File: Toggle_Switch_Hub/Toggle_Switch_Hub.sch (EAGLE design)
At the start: 6 parts

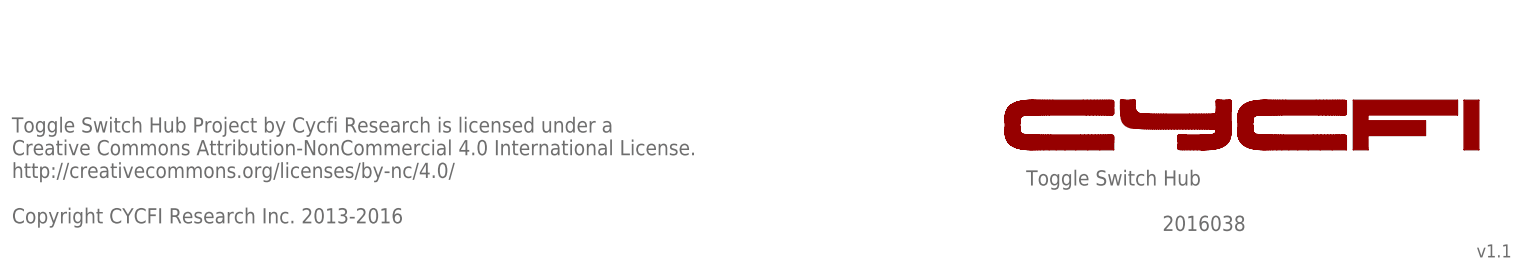
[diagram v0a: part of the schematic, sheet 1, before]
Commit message: Updated schematic licenses
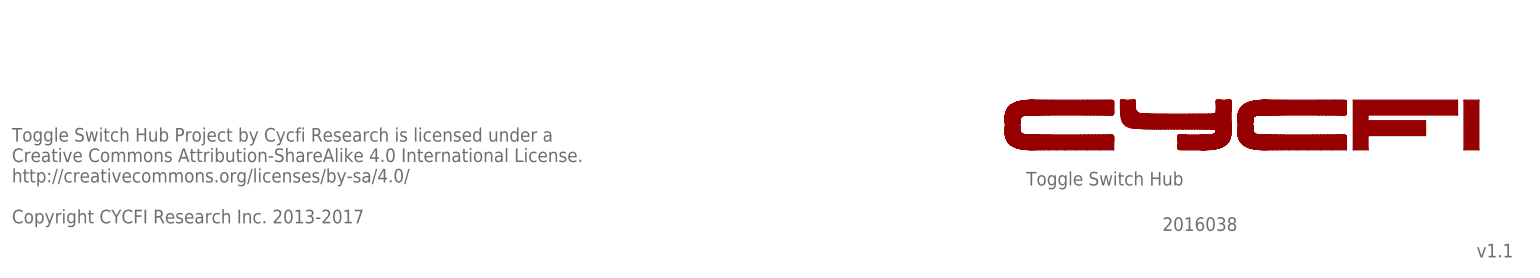
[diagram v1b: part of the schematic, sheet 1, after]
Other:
- note added: "Toggle Switch Hub Project by Cycfi Research is licensed under a Creative Commons Attribution-ShareAlike 4.0 International License. http://creativecommons.org/licenses/by-sa/4.0/ Copyright CYCFI Research Inc. 2013-2017"
- note removed: "Toggle Switch Hub Project by Cycfi Research is licensed under a Creative Commons Attribution-NonCommercial 4.0 International License. http://creativecommons.org/licenses/by-nc/4.0/ Copyright CYCFI Research Inc. 2013-2016"
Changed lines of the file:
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@@
 <text x="46.99" y="80.01" size="1.778" layer="95">STRING
 GND</text>
-<text x="177.8" y="19.05" size="2.54" layer="95">Toggle Switch Hub</text>
-<text x="253.365" y="6.985" size="2.1844" layer="95">v1.1</text>
-<text x="7.62" y="12.7" size="2.54" layer="95">Toggle Switch Hub Project by Cycfi Research is licensed under a
-Creative Commons Attribution-NonCommercial 4.0 International License.
-http://creativecommons.org/licenses/by-nc/4.0/
-Copyright CYCFI Research Inc. 2013-2016</text>
-<text x="200.66" y="11.43" size="2.54" layer="95">2016038</text>
+<text x="177.8" y="19.05" size="2.286" layer="95">Toggle Switch Hub</text>
+<text x="253.365" y="6.985" size="2.286" layer="95">v1.1</text>
+<text x="7.62" y="12.7" size="2.286" layer="95" font="fixed">Toggle Switch Hub Project by Cycfi Research is licensed under a
+Creative Commons Attribution-ShareAlike 4.0 International License.
+http://creativecommons.org/licenses/by-sa/4.0/
+Copyright CYCFI Research Inc. 2013-2017</text>
+<text x="200.66" y="11.43" size="2.286" layer="95">2016038</text>
 <wire x1="192.47528125" y1="25.047221875" x2="190.115640625" y2="25.047221875" width="0" layer="94"/>
 <wire x1="190.115640625" y1="25.047221875" x2="188.10833125" y2="25.047225" width="0" layer="94"/>
@@
 <instance part="FRAME3" gate="G$1" x="0" y="0"/>
 <instance part="FRAME3" gate="G$2" x="162.56" y="0" smashed="yes">
-<attribute name="LAST_DATE_TIME" x="175.26" y="1.27" size="2.54" layer="94" font="vector"/>
-<attribute name="SHEET" x="248.92" y="1.27" size="2.54" layer="94" font="vector"/>
+<attribute name="LAST_DATE_TIME" x="175.26" y="1.27" size="2.286" layer="94" font="vector"/>
+<attribute name="SHEET" x="248.92" y="1.27" size="2.286" layer="94" font="vector"/>
 </instance>
 </instances>
@@
 <text x="193.04" y="103.505" size="1.778" layer="95">VOL</text>
 <text x="193.675" y="94.615" size="1.778" layer="95">INS</text>
-<text x="178.435" y="19.685" size="2.54" layer="95">Toggle Switch Hub</text>
-<text x="254" y="7.62" size="2.1844" layer="95">v1.1</text>
-<text x="8.255" y="13.335" size="2.54" layer="95">Toggle Switch Hub Project by Cycfi Research is licensed under a
-Creative Commons Attribution-NonCommercial 4.0 International License.
-http://creativecommons.org/licenses/by-nc/4.0/
-Copyright CYCFI Research Inc. 2013-2016</text>
-<text x="201.295" y="12.065" size="2.54" layer="95">2016038</text>
+<text x="178.435" y="19.685" size="2.54" layer="95" font="fixed">Toggle Switch Hub</text>
+<text x="254" y="7.62" size="2.1844" layer="95" font="fixed">v1.1</text>
+<text x="8.255" y="13.335" size="2.54" layer="95" font="fixed">Toggle Switch Hub Project by Cycfi Research is licensed under a
+Creative Commons Attribution-ShareAlike 4.0 International License.
+http://creativecommons.org/licenses/by-sa/4.0/
+Copyright CYCFI Research Inc. 2013-2017</text>
+<text x="201.295" y="12.065" size="2.54" layer="95" font="fixed">2016038</text>
 <wire x1="193.11028125" y1="25.682221875" x2="190.750640625" y2="25.682221875" width="0" layer="94"/>
 <wire x1="190.750640625" y1="25.682221875" x2="188.74333125" y2="25.682225" width="0" layer="94"/>
@@
 <instance part="FRAME1" gate="G$1" x="0.635" y="0.635"/>
 <instance part="FRAME1" gate="G$2" x="163.195" y="0.635" smashed="yes">
-<attribute name="LAST_DATE_TIME" x="175.895" y="1.905" size="2.54" layer="94" font="vector"/>
-<attribute name="SHEET" x="249.555" y="1.905" size="2.54" layer="94" font="vector"/>
+<attribute name="LAST_DATE_TIME" x="175.895" y="1.905" size="2.54" layer="94" font="fixed"/>
+<attribute name="SHEET" x="249.555" y="1.905" size="2.54" layer="94" font="fixed"/>
 </instance>
 </instances>
